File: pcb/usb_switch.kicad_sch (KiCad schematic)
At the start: 1 part, among them U2 FE1.1s

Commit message: Schematic design
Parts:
- added C18, C19, C20: 10u, Capacitor_SMD:C_1206_3216Metric_Pad1.33x1.80mm_HandSolder, symbol Device:C
- added J4: Conn_01x04_Socket, Connector_JST:JST_PH_B4B-PH-K_1x04_P2.00mm_Vertical, symbol Connector:Conn_01x04_Socket
- added R10: 47k, Resistor_SMD:R_0603_1608Metric_Pad0.98x0.95mm_HandSolder, symbol Device:R
- added R11, R12, R13: 100k, Resistor_SMD:R_0603_1608Metric_Pad0.98x0.95mm_HandSolder, symbol Device:R
- added R14: 330, Resistor_SMD:R_0603_1608Metric_Pad0.98x0.95mm_HandSolder, symbol Device:R
- added R9: 2k7, Resistor_SMD:R_0603_1608Metric_Pad0.98x0.95mm_HandSolder, symbol Device:R
- added TP3: TestPoint, TestPoint:TestPoint_Pad_D1.0mm, symbol Connector:TestPoint
- added U4: 24LC02, Package_SO:SOIC-8_3.9x4.9mm_P1.27mm, symbol Memory_EEPROM:24LC02
- added Y1: ABM8G-12.000MHZ-18, Crystal:Crystal_SMD_Abracon_ABM8G-4Pin_3.2x2.5mm, symbol Device:Crystal_GND24
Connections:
- net GND: now reaches U2.1 (VSS)
- net GND: now also C18.2, C19.2, C20.2, J4.4 (Pin_4), R11.2, R9.1, Y1.2, Y1.4
- net D1-: now reaches U2.10 (DM1)
- net D1+: now reaches U2.11 (DP1)
- net at U2.12 (VD18_O): now also U2.28 (VD18), C20.1
- net 3V3USB: now reaches U2.13 (VD33)
- net 3V3USB: now also U2.21 (VD33_O), U2.26 (OVCJ), C19.1, R12.1, R13.1
- net at U2.14 (REXT): now also R9.2
- net D-: now reaches U2.15 (DMU)
- net D-: now also J4.3 (Pin_3)
- net D+: now reaches U2.16 (DPU)
- net D+: now also J4.2 (Pin_2)
- net at U2.17 (~{XRSTJ}): now also R13.2
- net at U2.18 (VBUSM): now also U2.20 (VDD5), C18.1, R10.1, R11.1
- net at U2.19 (BUSJ): now also R12.2
- net at U2.2 (XOUT): now also Y1.3
- net at U2.3 (XIN): now also Y1.1
- net D4-: now reaches U2.4 (DM4)
- net D4+: now reaches U2.5 (DP4)
- net D3-: now reaches U2.6 (DM3)
- net D3+: now reaches U2.7 (DP3)
- net D2-: now reaches U2.8 (DM2)
- net D2+: now reaches U2.9 (DP2)
- new net VUSB: J4.1 (Pin_1), R10.2, TP3.1
- no-connect marks 0 -> 1

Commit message: More schematic
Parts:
- added C21, C22: 100n, Capacitor_SMD:C_0603_1608Metric_Pad1.08x0.95mm_HandSolder, symbol Device:C
- added D2, D?: ~, LED_SMD:LED_0603_1608Metric_Pad1.05x0.95mm_HandSolder, symbol Device:LED
- added JP3: SolderJumper_3_Bridged12, Jumper:SolderJumper-3_P1.3mm_Bridged12_Pad1.0x1.5mm, symbol Jumper:SolderJumper_3_Bridged12
- added R15, R16: 10k, Resistor_SMD:R_0603_1608Metric_Pad0.98x0.95mm_HandSolder, symbol Device:R
- added R17, R18: 330, Resistor_SMD:R_0603_1608Metric_Pad0.98x0.95mm_HandSolder, symbol Device:R
- U4: now not fitted; now left out of the parts list
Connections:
- net 3V3USB: now also R14.2, U4.8 (VCC), C22.1, JP3.1 (A), R15.2, R16.2, R17.2
- net GND: now also U4.1 (A0), U4.2 (A1), U4.3 (A2), U4.4 (GND), C21.2, C22.2, JP3.3 (B), R18.1
- net at C18.1, R10.1, R11.1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: now also C21.1
- net at U2.22 (DRV): now also D2.2 (A)
- net at U2.23 (LED1/EESCL): now also U4.6 (SCL), D?.1 (K), R16.1
- net at U2.24 (LED2): now also R17.1
- net at U2.27 (TESTJ/EESDA): now also U4.5 (SDA), R15.1
- net at R14.1: now also D?.2 (A)
- net at U4.7 (WP): now also JP3.2 (C)
- new net: D2.1 (K), R18.2
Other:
- moved on the sheet: R14

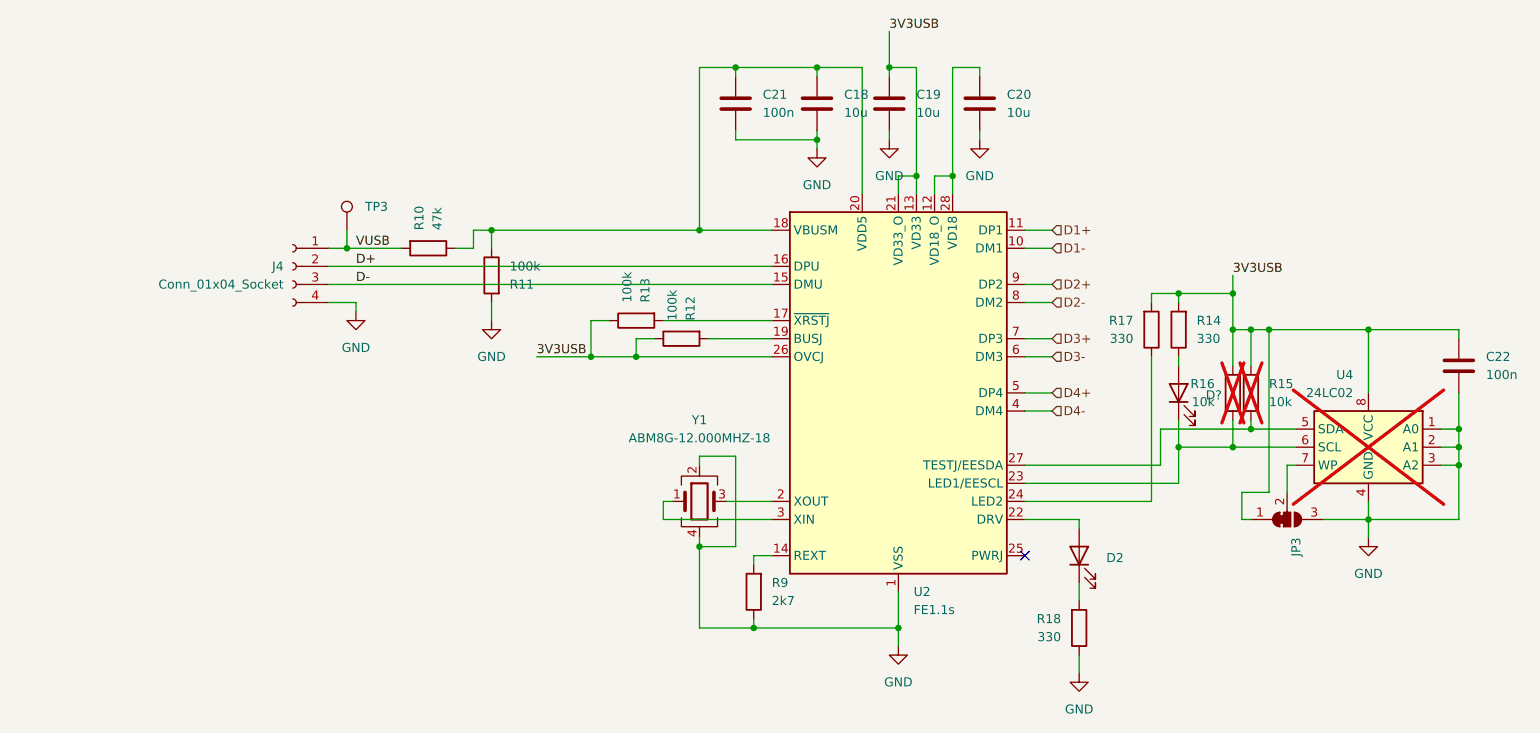
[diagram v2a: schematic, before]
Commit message: Sch complete, starting pcb
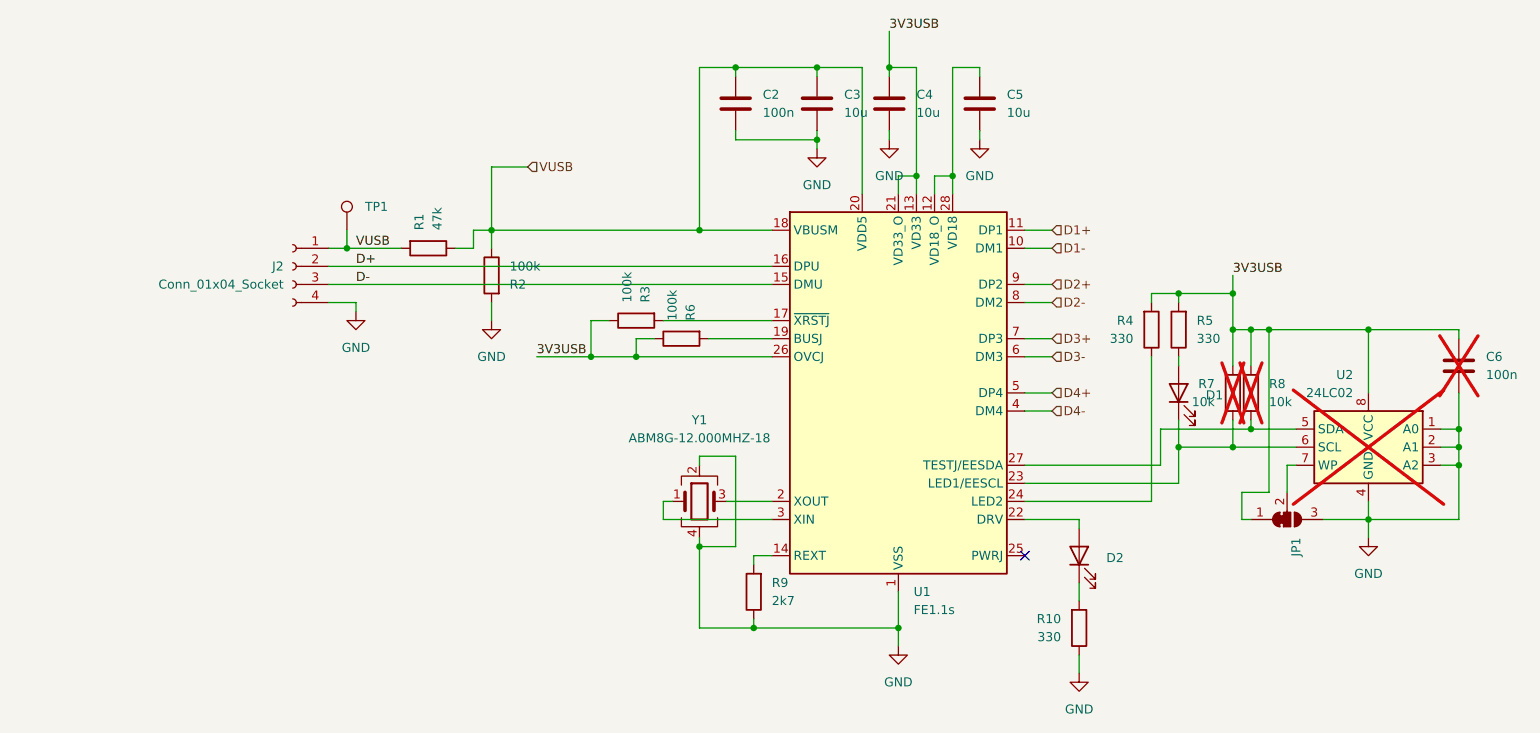
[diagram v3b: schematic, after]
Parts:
- C6: renamed from C22; now not fitted; now left out of the parts list
- gave numbers to parts that had none: 1
- renumbered C21 to C2, C18 to C3, C19 to C4, C20 to C5, J4 to J2, JP3 to JP1, R10 to R1, R18 to R10, R11 to R2, R13 to R3, R17 to R4, R14 to R5, R12 to R6, R16 to R7, R15 to R8, TP3 to TP1, U2 to U1, U4 to U2
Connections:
- net VUSB: now also C2.1, C3.1, R1.1, R2.1, U1.18 (VBUSM), U1.20 (VDD5)
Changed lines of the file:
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@@
 	(wire
 		(pts
+			(xy 85.09 67.31) (xy 85.09 58.42)
+		)
+		(stroke
+			(width 0)
+			(type default)
+		)
+	)
+	(wire
+		(pts
 			(xy 190.5 104.14) (xy 194.31 104.14)
 		)
@@
 	(wire
 		(pts
+			(xy 85.09 58.42) (xy 90.17 58.42)
+		)
+		(stroke
+			(width 0)
+			(type default)
+		)
+	)
+	(wire
+		(pts
 			(xy 189.23 73.66) (xy 189.23 76.2)
 		)
@@
 		)
 	)
+	(hierarchical_label "VUSB"
+		(shape input)
+		(at 90.17 58.42 0)
+		(effects
+			(font
+				(size 1.27 1.27)
+			)
+			(justify left)
+		)
+	)
 	(hierarchical_label "D4-"
 		(shape input)
@@
 		(dnp no)
 		(fields_autoplaced yes)
-		(property "Reference" "C18"
+		(property "Reference" "C3"
 			(at 134.62 48.2599 0)
 			(effects
@@
 			(project "QCB_board"
 				(path "/3a9957e4-3d4a-4c65-a0c0-c287bc2a56fb/82a26402-3849-46fd-a3a1-52c735998b36"
-					(reference "C18")
+					(reference "C3")
 					(unit 1)
 				)
@@
 		(on_board yes)
 		(dnp no)
-		(property "Reference" "J4"
+		(property "Reference" "J2"
 			(at 55.88 72.3899 0)
 			(effects
@@
 			(project "QCB_board"
 				(path "/3a9957e4-3d4a-4c65-a0c0-c287bc2a56fb/82a26402-3849-46fd-a3a1-52c735998b36"
-					(reference "J4")
+					(reference "J2")
 					(unit 1)
 				)
@@
 		(unit 1)
 		(exclude_from_sim no)
-		(in_bom yes)
+		(in_bom no)
 		(on_board yes)
-		(dnp no)
+		(dnp yes)
 		(fields_autoplaced yes)
-		(property "Reference" "C22"
+		(property "Reference" "C6"
 			(at 224.79 85.0899 0)
 			(effects
@@
 			(project "QCB_board"
 				(path "/3a9957e4-3d4a-4c65-a0c0-c287bc2a56fb/82a26402-3849-46fd-a3a1-52c735998b36"
-					(reference "C22")
+					(reference "C6")
 					(unit 1)
 				)
@@
 		(on_board yes)
 		(dnp no)
-		(property "Reference" "D?"
+		(property "Reference" "D1"
 			(at 185.42 90.4874 90)
 			(effects
@@
 			(project "QCB_board"
 				(path "/3a9957e4-3d4a-4c65-a0c0-c287bc2a56fb/82a26402-3849-46fd-a3a1-52c735998b36"
-					(reference "D?")
+					(reference "D1")
 					(unit 1)
 				)
@@
 		(dnp no)
 		(fields_autoplaced yes)
-		(property "Reference" "#PWR016"
+		(property "Reference" "#PWR05"
 			(at 140.97 60.96 0)
 			(effects
@@
 			(project "QCB_board"
 				(path "/3a9957e4-3d4a-4c65-a0c0-c287bc2a56fb/82a26402-3849-46fd-a3a1-52c735998b36"
-					(reference "#PWR016")
+					(reference "#PWR05")
 					(unit 1)
 				)
@@
 		(dnp no)
 		(fields_autoplaced yes)
-		(property "Reference" "#PWR013"
+		(property "Reference" "#PWR09"
 			(at 85.09 86.36 0)
 			(effects
@@
 			(project "QCB_board"
 				(path "/3a9957e4-3d4a-4c65-a0c0-c287bc2a56fb/82a26402-3849-46fd-a3a1-52c735998b36"
-					(reference "#PWR013")
+					(reference "#PWR09")
 					(unit 1)
 				)
@@
 		(dnp no)
 		(fields_autoplaced yes)
-		(property "Reference" "C21"
+		(property "Reference" "C2"
 			(at 123.19 48.2599 0)
 			(effects
@@
 			(project "QCB_board"
 				(path "/3a9957e4-3d4a-4c65-a0c0-c287bc2a56fb/82a26402-3849-46fd-a3a1-52c735998b36"
-					(reference "C21")
+					(reference "C2")
 					(unit 1)
 				)
@@
 		(on_board yes)
 		(dnp yes)
-		(property "Reference" "R16"
+		(property "Reference" "R7"
 			(at 186.69 88.8999 0)
 			(effects
@@
 			(project "QCB_board"
 				(path "/3a9957e4-3d4a-4c65-a0c0-c287bc2a56fb/82a26402-3849-46fd-a3a1-52c735998b36"
-					(reference "R16")
+					(reference "R7")
 					(unit 1)
 				)
@@
 		(dnp no)
 		(fields_autoplaced yes)
-		(property "Reference" "#PWR022"
+		(property "Reference" "#PWR012"
 			(at 167.64 135.89 0)
 			(effects
@@
 			(project "QCB_board"
 				(path "/3a9957e4-3d4a-4c65-a0c0-c287bc2a56fb/82a26402-3849-46fd-a3a1-52c735998b36"
-					(reference "#PWR022")
+					(reference "#PWR012")
 					(unit 1)
 				)
@@
 		(on_board yes)
 		(dnp no)
-		(property "Reference" "R18"
+		(property "Reference" "R10"
 			(at 165.1 121.9199 0)
 			(effects
@@
 			(project "QCB_board"
 				(path "/3a9957e4-3d4a-4c65-a0c0-c287bc2a56fb/82a26402-3849-46fd-a3a1-52c735998b36"
-					(reference "R18")
+					(reference "R10")
 					(unit 1)
 				)
@@
 		(on_board yes)
 		(dnp yes)
-		(property "Reference" "R15"
+		(property "Reference" "R8"
 			(at 194.31 88.8999 0)
 			(effects
@@
 			(project "QCB_board"
 				(path "/3a9957e4-3d4a-4c65-a0c0-c287bc2a56fb/82a26402-3849-46fd-a3a1-52c735998b36"
-					(reference "R15")
+					(reference "R8")
 					(unit 1)
 				)
@@
 		(dnp no)
 		(fields_autoplaced yes)
-		(property "Reference" "U2"
+		(property "Reference" "U1"
 			(at 144.3833 118.11 0)
 			(effects
@@
 			(project ""
 				(path "/3a9957e4-3d4a-4c65-a0c0-c287bc2a56fb/82a26402-3849-46fd-a3a1-52c735998b36"
-					(reference "U2")
+					(reference "U1")
 					(unit 1)
 				)
@@
 		(dnp no)
 		(fields_autoplaced yes)
-		(property "Reference" "#PWR023"
+		(property "Reference" "#PWR08"
 			(at 66.04 85.09 0)
 			(effects
@@
 			(project "QCB_board"
 				(path "/3a9957e4-3d4a-4c65-a0c0-c287bc2a56fb/82a26402-3849-46fd-a3a1-52c735998b36"
-					(reference "#PWR023")
+					(reference "#PWR08")
 					(unit 1)
 				)
@@
 		(on_board yes)
 		(dnp no)
-		(property "Reference" "R11"
+		(property "Reference" "R2"
 			(at 87.63 74.9301 0)
 			(effects
@@
 			(project "QCB_board"
 				(path "/3a9957e4-3d4a-4c65-a0c0-c287bc2a56fb/82a26402-3849-46fd-a3a1-52c735998b36"
-					(reference "R11")
+					(reference "R2")
 					(unit 1)
 				)
@@
 		(on_board yes)
 		(dnp no)
-		(property "Reference" "JP3"
+		(property "Reference" "JP1"
 			(at 198.1201 110.49 90)
 			(effects
@@
 			(project "QCB_board"
 				(path "/3a9957e4-3d4a-4c65-a0c0-c287bc2a56fb/82a26402-3849-46fd-a3a1-52c735998b36"
-					(reference "JP3")
+					(reference "JP1")
 					(unit 1)
 				)
@@
 		(on_board yes)
 		(dnp no)
-		(property "Reference" "R17"
+		(property "Reference" "R4"
 			(at 175.26 80.0099 0)
 			(effects
@@
 			(project "QCB_board"
 				(path "/3a9957e4-3d4a-4c65-a0c0-c287bc2a56fb/82a26402-3849-46fd-a3a1-52c735998b36"
-					(reference "R17")
+					(reference "R4")
 					(unit 1)
 				)
@@
 		(on_board yes)
 		(dnp no)
-		(property "Reference" "R12"
+		(property "Reference" "R6"
 			(at 113.0301 80.01 0)
 			(effects
@@
 			(project "QCB_board"
 				(path "/3a9957e4-3d4a-4c65-a0c0-c287bc2a56fb/82a26402-3849-46fd-a3a1-52c735998b36"
-					(reference "R12")
+					(reference "R6")
 					(unit 1)
 				)
@@
 		(on_board yes)
 		(dnp no)
-		(property "Reference" "R14"
+		(property "Reference" "R5"
 			(at 184.15 80.0099 0)
 			(effects
@@
 			(project "QCB_board"
 				(path "/3a9957e4-3d4a-4c65-a0c0-c287bc2a56fb/82a26402-3849-46fd-a3a1-52c735998b36"
-					(reference "R14")
+					(reference "R5")
 					(unit 1)
 				)
@@
 		(dnp no)
 		(fields_autoplaced yes)
-		(property "Reference" "#PWR014"
+		(property "Reference" "#PWR07"
 			(at 130.81 62.23 0)
 			(effects
@@
 			(project "QCB_board"
 				(path "/3a9957e4-3d4a-4c65-a0c0-c287bc2a56fb/82a26402-3849-46fd-a3a1-52c735998b36"
-					(reference "#PWR014")
+					(reference "#PWR07")
 					(unit 1)
 				)
@@
 		(dnp no)
 		(fields_autoplaced yes)
-		(property "Reference" "#PWR012"
+		(property "Reference" "#PWR011"
 			(at 142.24 132.08 0)
 			(effects
@@
 			(project "QCB_board"
 				(path "/3a9957e4-3d4a-4c65-a0c0-c287bc2a56fb/82a26402-3849-46fd-a3a1-52c735998b36"
-					(reference "#PWR012")
+					(reference "#PWR011")
 					(unit 1)
 				)
@@
 		(dnp no)
 		(fields_autoplaced yes)
-		(property "Reference" "TP3"
+		(property "Reference" "TP1"
 			(at 67.31 64.0079 0)
 			(effects
@@
 			(project "QCB_board"
 				(path "/3a9957e4-3d4a-4c65-a0c0-c287bc2a56fb/82a26402-3849-46fd-a3a1-52c735998b36"
-					(reference "TP3")
+					(reference "TP1")
 					(unit 1)
 				)
@@
 		(dnp yes)
 		(fields_autoplaced yes)
-		(property "Reference" "U4"
+		(property "Reference" "U2"
 			(at 206.1367 87.63 0)
 			(effects
@@
 			(project ""
 				(path "/3a9957e4-3d4a-4c65-a0c0-c287bc2a56fb/82a26402-3849-46fd-a3a1-52c735998b36"
-					(reference "U4")
+					(reference "U2")
 					(unit 1)
 				)
@@
 		(on_board yes)
 		(dnp no)
-		(property "Reference" "R13"
+		(property "Reference" "R3"
 			(at 106.6801 77.47 0)
 			(effects
@@
 			(project "QCB_board"
 				(path "/3a9957e4-3d4a-4c65-a0c0-c287bc2a56fb/82a26402-3849-46fd-a3a1-52c735998b36"
-					(reference "R13")
+					(reference "R3")
 					(unit 1)
 				)
@@
 		(dnp no)
 		(fields_autoplaced yes)
-		(property "Reference" "C20"
+		(property "Reference" "C5"
 			(at 157.48 48.2599 0)
 			(effects
@@
 			(project "QCB_board"
 				(path "/3a9957e4-3d4a-4c65-a0c0-c287bc2a56fb/82a26402-3849-46fd-a3a1-52c735998b36"
-					(reference "C20")
+					(reference "C5")
 					(unit 1)
 				)
@@
 		(dnp no)
 		(fields_autoplaced yes)
-		(property "Reference" "#PWR017"
+		(property "Reference" "#PWR06"
 			(at 153.67 60.96 0)
 			(effects
@@
 			(project "QCB_board"
 				(path "/3a9957e4-3d4a-4c65-a0c0-c287bc2a56fb/82a26402-3849-46fd-a3a1-52c735998b36"
-					(reference "#PWR017")
+					(reference "#PWR06")
 					(unit 1)
 				)
@@
 		(dnp no)
 		(fields_autoplaced yes)
-		(property "Reference" "#PWR024"
+		(property "Reference" "#PWR010"
 			(at 208.28 116.84 0)
 			(effects
@@
 			(project "QCB_board"
 				(path "/3a9957e4-3d4a-4c65-a0c0-c287bc2a56fb/82a26402-3849-46fd-a3a1-52c735998b36"
-					(reference "#PWR024")
+					(reference "#PWR010")
 					(unit 1)
 				)
@@
 		(on_board yes)
 		(dnp no)
-		(property "Reference" "R10"
+		(property "Reference" "R1"
 			(at 74.9299 67.31 0)
 			(effects
@@
 			(project "QCB_board"
 				(path "/3a9957e4-3d4a-4c65-a0c0-c287bc2a56fb/82a26402-3849-46fd-a3a1-52c735998b36"
-					(reference "R10")
+					(reference "R1")
 					(unit 1)
 				)
@@
 		(dnp no)
 		(fields_autoplaced yes)
-		(property "Reference" "C19"
+		(property "Reference" "C4"
 			(at 144.78 48.2599 0)
 			(effects
@@
 			(project "QCB_board"
 				(path "/3a9957e4-3d4a-4c65-a0c0-c287bc2a56fb/82a26402-3849-46fd-a3a1-52c735998b36"
-					(reference "C19")
+					(reference "C4")
 					(unit 1)
 				)

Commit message: Routing
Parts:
- added U14: USBLC6-2SC6, Package_TO_SOT_SMD:SOT-23-6_Handsoldering, symbol Power_Protection:USBLC6-2SC6
- R1: value 47k -> 0R/47k
- R2: now not fitted; now left out of the parts list
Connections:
- net D+: now also U14.6 (I/O1); no longer J2.2 (Pin_2)
- net D-: now also U14.4 (I/O2); no longer J2.3 (Pin_3)
- net GND: now also U14.2 (GND)
- net VUSB: now also U14.5 (VBUS); no longer R1.1, R2.1, U1.18 (VBUSM)
- new net: R1.1, R2.1, U1.18 (VBUSM)
- new net D_N: J2.3 (Pin_3), U14.3 (I/O2)
- new net D_P: J2.2 (Pin_2), U14.1 (I/O1)
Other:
- moved on the sheet: J2, TP1
